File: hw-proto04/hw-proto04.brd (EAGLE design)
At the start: 54.3 x 58.4 mm, 31 parts, among them IC2 UCC27523DR, IC3 MCP2562T, IC4 STM32F042C6T7, IC5 TLV74333PDBVR, J1 10, J2 10, Q1 SQJ147ELP-T1_GE3, Q2 SQJ147ELP-T1_GE3

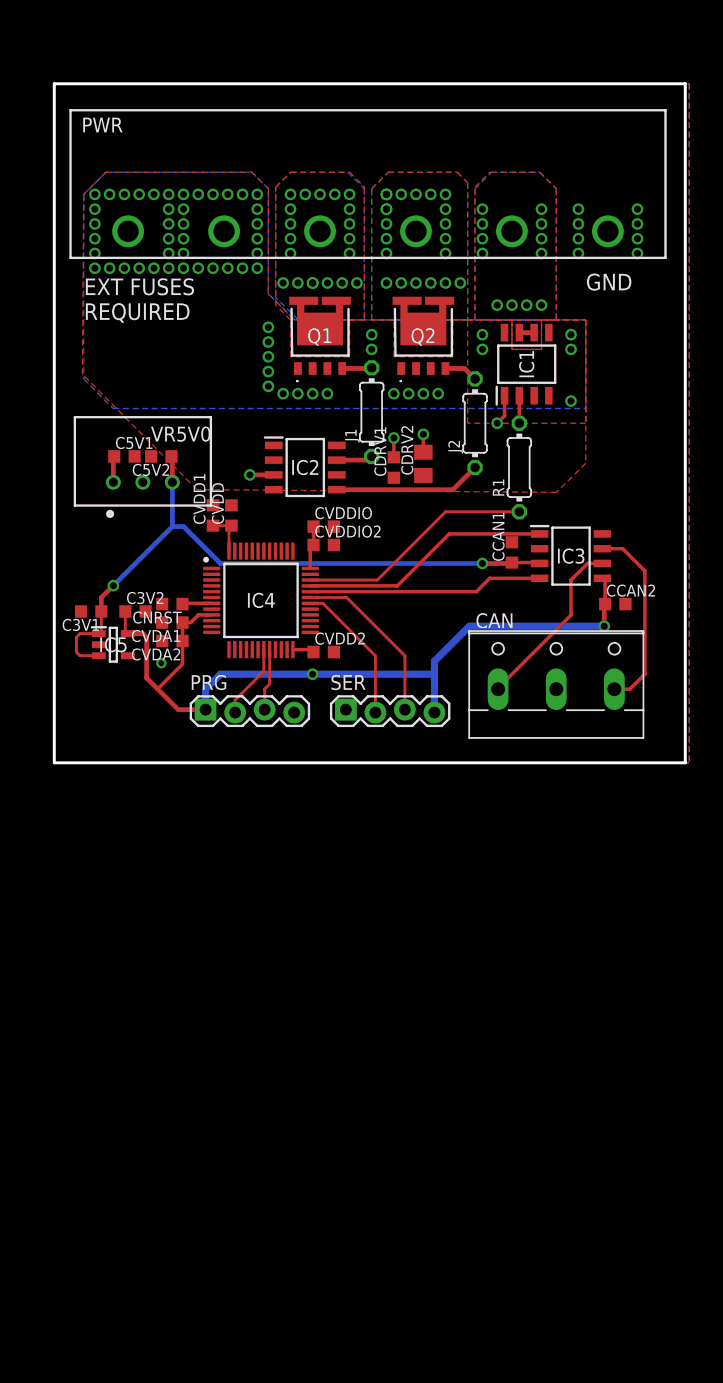
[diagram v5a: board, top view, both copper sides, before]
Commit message: added VBAT divider, refinements
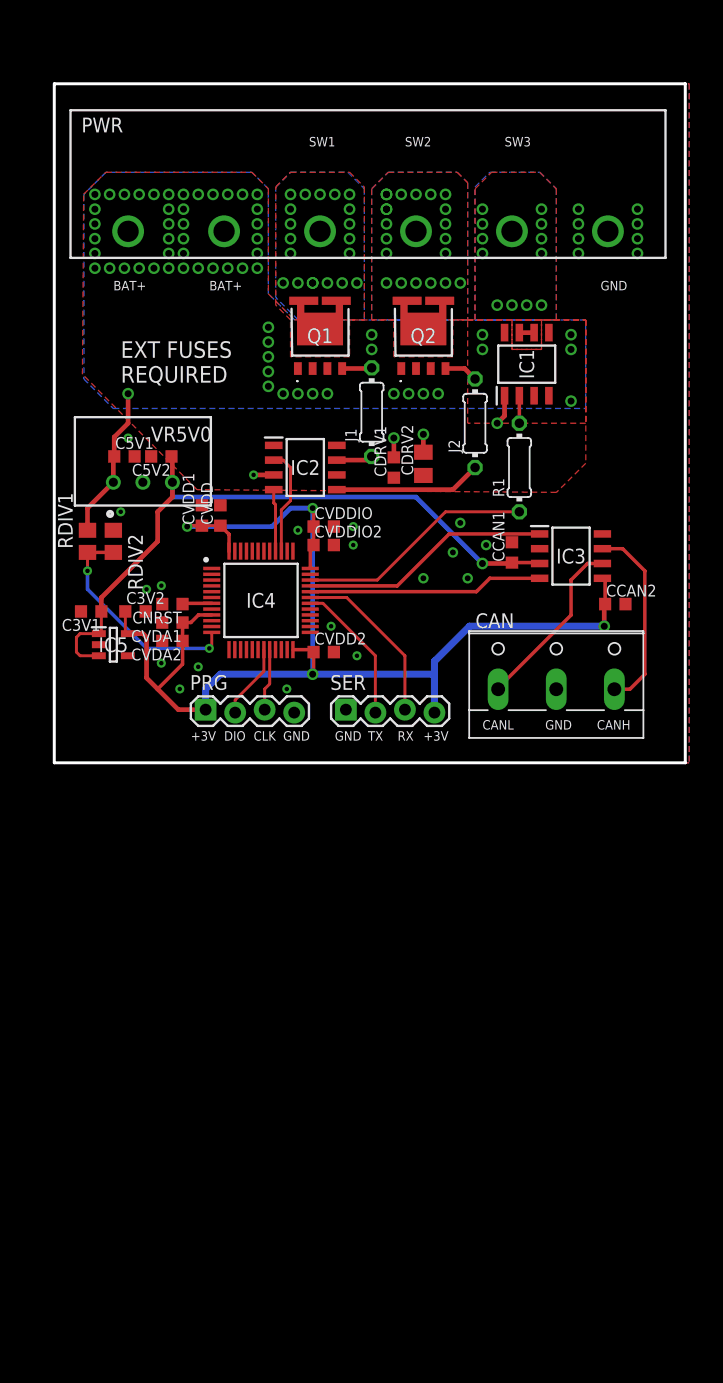
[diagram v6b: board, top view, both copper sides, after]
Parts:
- added RDIV1, RDIV2: (no value), rcl:R0805
- moved CVDD 0.95 mm to (15.6, 21.3)
- moved CVDD1 0.95 mm to (14.0, 21.3)
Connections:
- net N$1 renamed CANH
- net N$2 renamed CANL
- new net ADC2: IC4.12, RDIV1.1, RDIV2.2
- net +12V: now also RDIV1.2
- net GND: now also RDIV2.1
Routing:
- net +3V3: track 79.0 -> 109.7 mm, vias 2 -> 4
- net ADC2: track 0.00 -> 19.4 mm, vias 0 -> 2
- net +12V: track 2.30 -> 13.2 mm, vias 60 -> 61
- net CTL1: track 0.00 -> 9.22 mm
- net CTL2: track 0.00 -> 5.35 mm
- net +5V: track 56.3 -> 58.7 mm, vias 2 -> 1
- net GND: track 7.89 -> 7.57 mm, vias 13 -> 30
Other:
- board text added: "+3V"
- board text added: "BAT+"
- board text added: "CANH"
- board text added: "CANL"
- board text added: "CLK"
- board text added: "DIO"
- board text added: "RX"
- board text added: "SW1"
- board text added: "SW2"
- board text added: "SW3"
- board text added: "TX"

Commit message: refinements
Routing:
- net GND: vias 30 -> 34
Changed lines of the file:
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@@
 <via x="9.2075" y="14.9225" extent="1-16" drill="0.381"/>
 <via x="10.4775" y="15.24" extent="1-16" drill="0.381"/>
-<via x="38.4175" y="18.7325" extent="1-16" drill="0.5"/>
 <via x="35.56" y="18.0975" extent="1-16" drill="0.5"/>
 <via x="36.83" y="15.875" extent="1-16" drill="0.5"/>
@@
 <via x="12.065" y="6.35" extent="1-16" drill="0.381"/>
 <via x="6.985" y="21.59" extent="1-16" drill="0.381"/>
+<via x="50.8" y="11.7475" extent="1-16" drill="0.381"/>
+<via x="38.4175" y="18.7325" extent="1-16" drill="0.381"/>
+<via x="17.145" y="21.9075" extent="1-16" drill="0.381"/>
+<via x="11.7475" y="21.2725" extent="1-16" drill="0.381"/>
+<via x="50.4825" y="16.1925" extent="1-16" drill="0.381"/>
 </signal>
 <signal name="SW1">

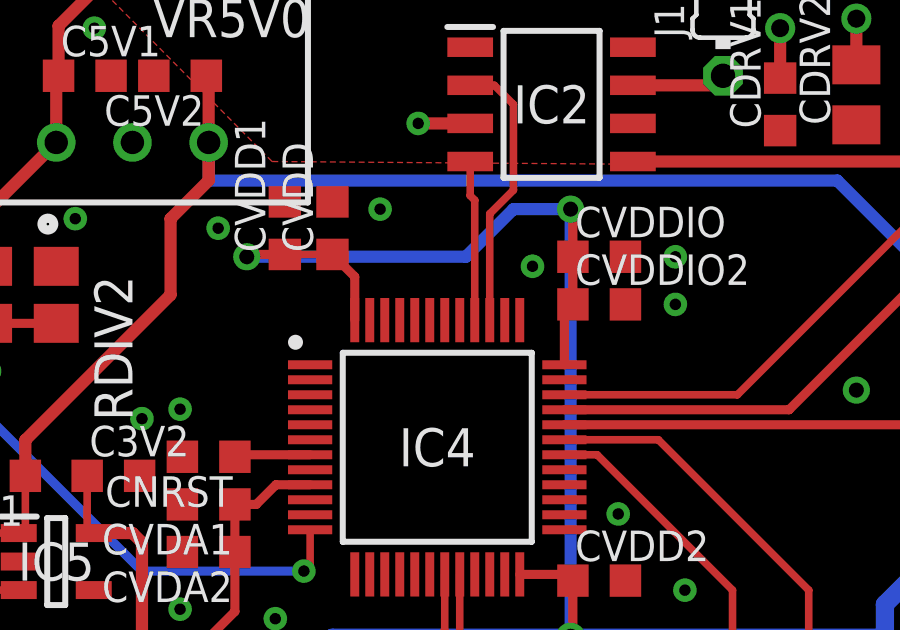
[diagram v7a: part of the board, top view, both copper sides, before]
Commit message: added boot0 pulldown
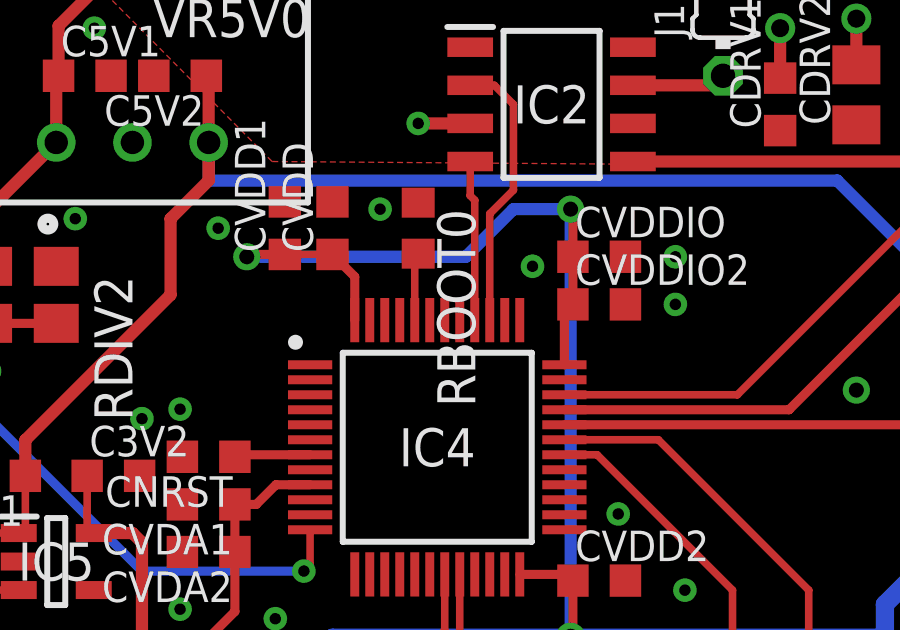
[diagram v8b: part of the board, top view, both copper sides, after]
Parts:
- added RBOOT0: 100K, rcl:R0603
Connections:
- new net BOOT0: IC4.44, RBOOT0.2
- net GND: now also RBOOT0.1
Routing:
- net BOOT0: track 0.00 -> 2.26 mm
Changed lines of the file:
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@@
 <element name="RDIV1" library="rcl" package="R0805" value="" x="4.1275" y="19.05" rot="R90"/>
 <element name="RDIV2" library="rcl" package="R0805" value="" x="6.35" y="19.05" rot="R270"/>
+<element name="RBOOT0" library="rcl" package="R0603" value="100K" x="18.415" y="21.2725" rot="R270"/>
 </elements>
 <signals>
@@
 <via x="11.7475" y="21.2725" extent="1-16" drill="0.381"/>
 <via x="50.4825" y="16.1925" extent="1-16" drill="0.381"/>
+<contactref element="RBOOT0" pad="1"/>
 </signal>
 <signal name="SW1">
@@
 <wire x1="6.35" y1="18.1" x2="4.1275" y2="18.1" width="0.3048" layer="1"/>
 </signal>
+<signal name="BOOT0">
+<contactref element="IC4" pad="44"/>
+<contactref element="RBOOT0" pad="2"/>
+<wire x1="18.3" y1="18.208" x2="18.3" y2="20.3075" width="0.254" layer="1"/>
+<wire x1="18.3" y1="20.3075" x2="18.415" y2="20.4225" width="0.254" layer="1"/>
+</signal>
 </signals>
